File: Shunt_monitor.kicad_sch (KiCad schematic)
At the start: 11 parts, among them U3 LM358

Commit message: completato il file pcb, creato un file gerber nella directory 'output' e creato i file pdf dello schema nella directory 'docs'
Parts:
- Creg1: footprint Capacitor_SMD:C_01005_0402Metric -> Capacitor_SMD:C_0402_1005Metric_Pad0.74x0.62mm_HandSolder
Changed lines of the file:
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@@
     (property "Reference" "Creg1" (id 0) (at 67.945 59.69 90))
     (property "Value" "0,1 uF" (id 1) (at 67.945 62.23 90))
-    (property "Footprint" "Capacitor_SMD:C_01005_0402Metric" (id 2) (at 71.755 65.7098 0)
+    (property "Footprint" "Capacitor_SMD:C_0402_1005Metric_Pad0.74x0.62mm_HandSolder" (id 2) (at 71.755 65.7098 0)
       (effects (font (size 1.27 1.27)) hide)
     )

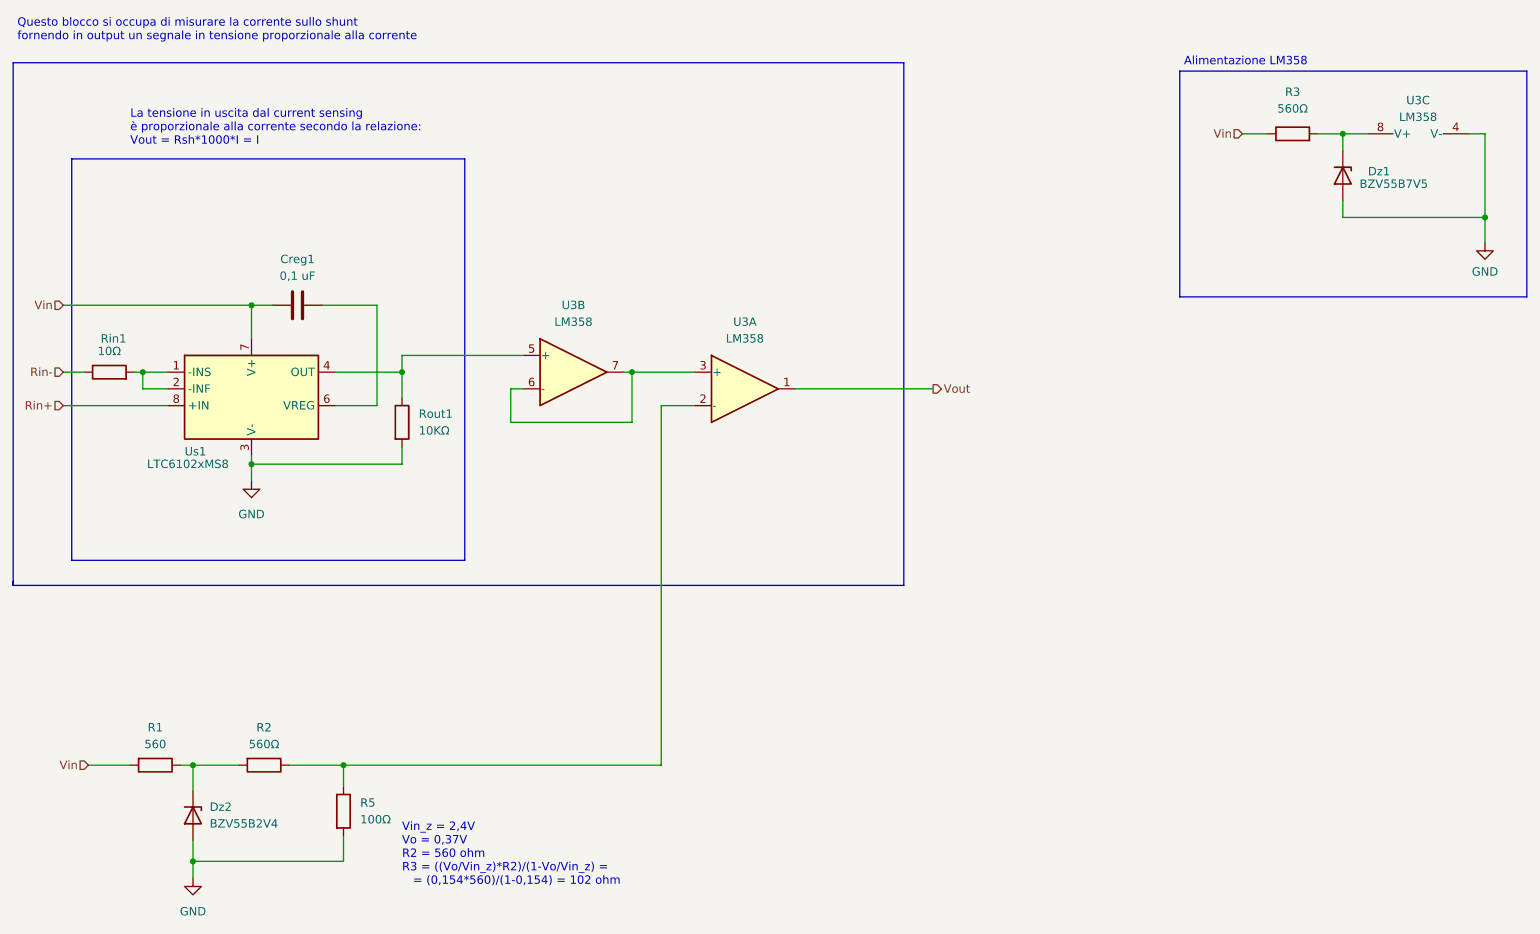
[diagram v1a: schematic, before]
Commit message: modificalo lo schematic e rifatto in parte il design PCB
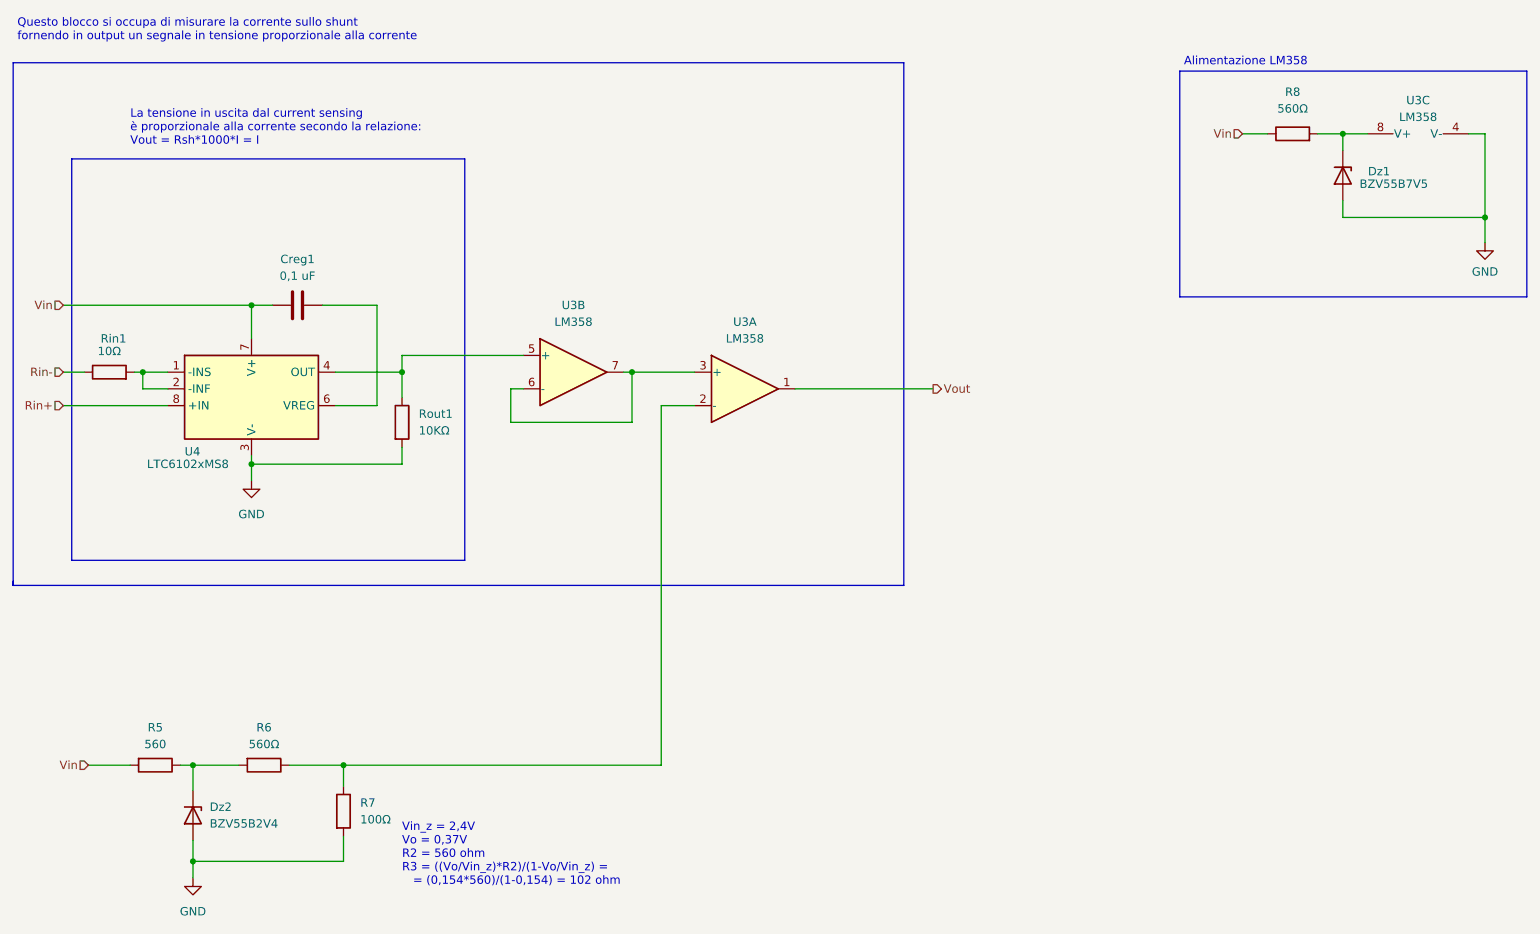
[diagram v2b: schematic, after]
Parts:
- renumbered R1 to R5, R2 to R6, R5 to R7, R3 to R8, Us1 to U4
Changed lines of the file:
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@@
   (symbol (lib_id "Device:R") (at 219.075 40.64 90) (unit 1)
     (in_bom yes) (on_board yes) (fields_autoplaced)
-    (property "Reference" "R3" (id 0) (at 219.075 34.29 90))
+    (property "Reference" "R8" (id 0) (at 219.075 34.29 90))
     (property "Value" "560Ω" (id 1) (at 219.075 36.83 90))
     (property "Footprint" "Resistor_SMD:R_0603_1608Metric" (id 2) (at 219.075 42.418 90)
@@
   (symbol (lib_id "Amplifier_Current:LTC6102xMS8") (at 60.96 81.915 0) (unit 1)
     (in_bom yes) (on_board yes)
-    (property "Reference" "Us1" (id 0) (at 50.8 88.9 0)
+    (property "Reference" "U4" (id 0) (at 50.8 88.9 0)
       (effects (font (size 1.27 1.27)) (justify left))
     )
@@
   (symbol (lib_id "Device:R") (at 46.355 136.525 270) (unit 1)
     (in_bom yes) (on_board yes) (fields_autoplaced)
-    (property "Reference" "R1" (id 0) (at 46.355 130.81 90))
+    (property "Reference" "R5" (id 0) (at 46.355 130.81 90))
     (property "Value" "560" (id 1) (at 46.355 133.35 90))
     (property "Footprint" "Resistor_SMD:R_0603_1608Metric" (id 2) (at 46.355 134.747 90)
@@
   (symbol (lib_id "Device:R") (at 74.93 143.51 0) (unit 1)
     (in_bom yes) (on_board yes) (fields_autoplaced)
-    (property "Reference" "R5" (id 0) (at 77.47 142.2399 0)
+    (property "Reference" "R7" (id 0) (at 77.47 142.2399 0)
       (effects (font (size 1.27 1.27)) (justify left))
     )
@@
   (symbol (lib_id "Device:R") (at 62.865 136.525 270) (unit 1)
     (in_bom yes) (on_board yes) (fields_autoplaced)
-    (property "Reference" "R2" (id 0) (at 62.865 130.81 90))
+    (property "Reference" "R6" (id 0) (at 62.865 130.81 90))
     (property "Value" "560Ω" (id 1) (at 62.865 133.35 90))
     (property "Footprint" "Resistor_SMD:R_0603_1608Metric" (id 2) (at 62.865 134.747 90)
